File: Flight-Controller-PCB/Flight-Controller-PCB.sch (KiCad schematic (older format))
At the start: 28 parts, among them J1 Power_In, J2 ESC_1, J3 ESC_2, J4 ESC_3, J5 ESC_4, J6 Receiver, J7 Aux, U1 MCP6001U

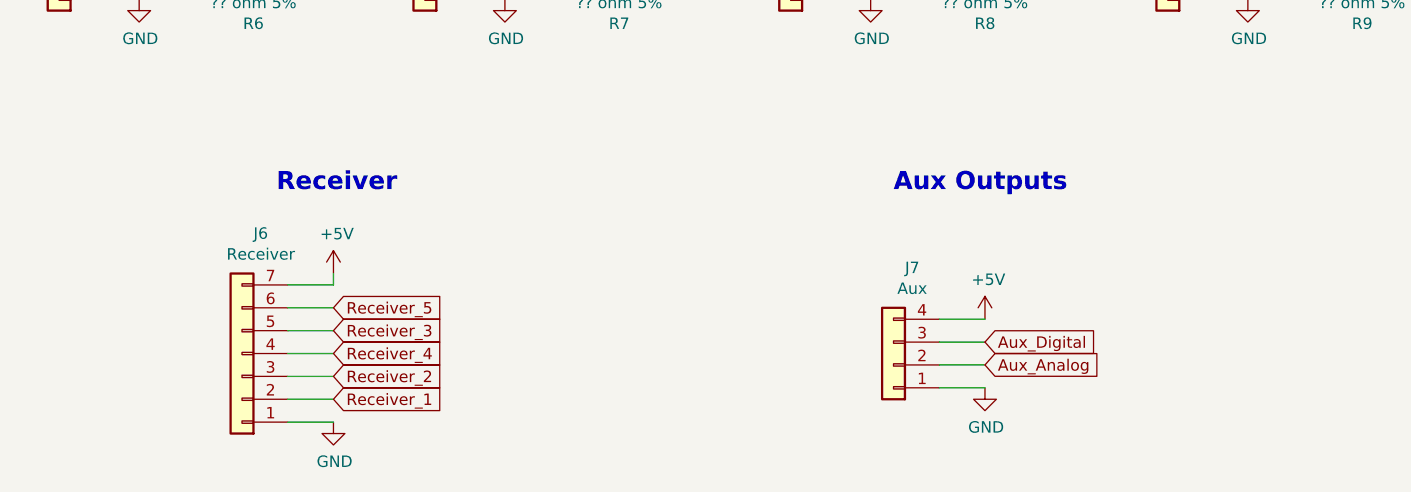
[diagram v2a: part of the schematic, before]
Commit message: Mostly finished off the schematic, need to double check and label
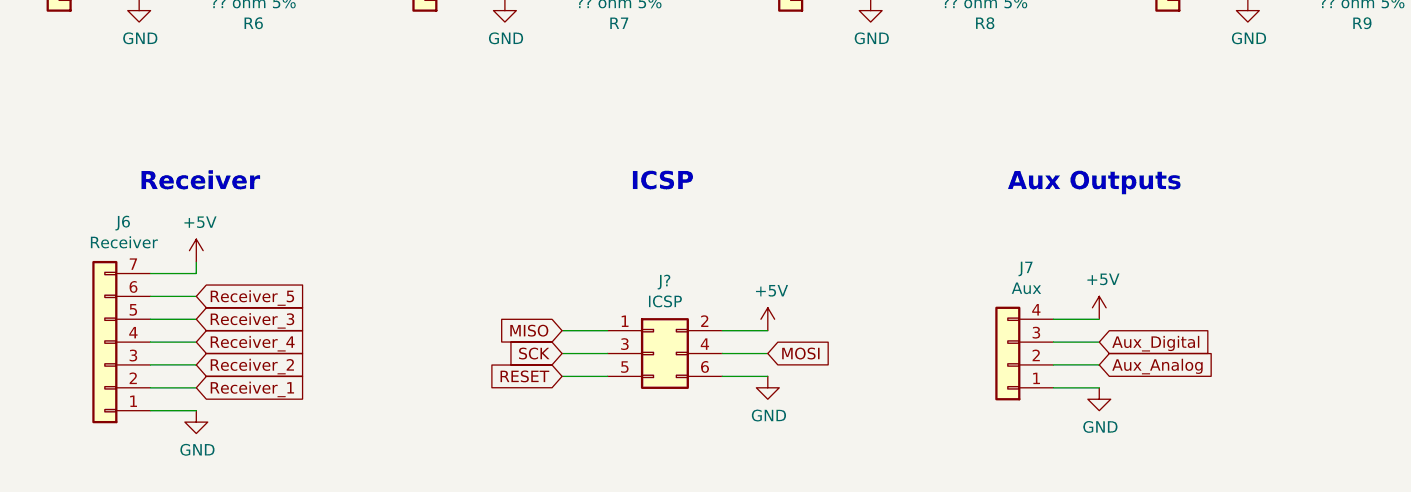
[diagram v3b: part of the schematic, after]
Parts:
- added J?: ICSP, symbol Connector_Generic:Conn_02x03_Odd_Even
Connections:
- net +5V: now also J?.2 (Pin_2)
- net GND: now also J?.6 (Pin_6)
- new net MISO: J?.1 (Pin_1)
- new net MOSI: J?.4 (Pin_4)
- new net RESET: J?.5 (Pin_5)
- new net SCK: J?.3 (Pin_3)
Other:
- note added: "ICSP"
- moved on the sheet: J6, J7
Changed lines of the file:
@@
 EESchema Schematic File Version 4
+LIBS:Flight-Controller-PCB-cache
 EELAYER 30 0
 EELAYER END
@@
 Text Label 1500 4100 0    50   ~ 0
 ESC_4
-Text Notes 1700 6500 0    79   ~ 16
+Text Notes 1100 6500 0    79   ~ 16
 Receiver
-Text GLabel 1950 7400 2    50   Input ~ 0
+Text GLabel 1350 7350 2    50   Input ~ 0
 Receiver_1
-Text GLabel 1950 7300 2    50   Input ~ 0
+Text GLabel 1350 7250 2    50   Input ~ 0
 Receiver_2
-Text GLabel 1950 7100 2    50   Input ~ 0
+Text GLabel 1350 7050 2    50   Input ~ 0
 Receiver_3
-Text GLabel 1950 7200 2    50   Input ~ 0
+Text GLabel 1350 7150 2    50   Input ~ 0
 Receiver_4
 $Comp
 L power:+5V #PWR018
 U 1 1 5FE81BA9
-P 1950 6850
-F 0 "#PWR018" H 1950 6700 50  0001 C CNN
-F 1 "+5V" H 1965 7023 50  0000 C CNN
-F 2 "" H 1950 6850 50  0001 C CNN
-F 3 "" H 1950 6850 50  0001 C CNN
-	1    1950 6850
+P 1350 6800
+F 0 "#PWR018" H 1350 6650 50  0001 C CNN
+F 1 "+5V" H 1365 6973 50  0000 C CNN
+F 2 "" H 1350 6800 50  0001 C CNN
+F 3 "" H 1350 6800 50  0001 C CNN
+	1    1350 6800
 	1    0    0    -1
 $EndComp
@@
 L power:GND #PWR021
 U 1 1 5FE821AC
-P 1950 7500
-F 0 "#PWR021" H 1950 7250 50  0001 C CNN
-F 1 "GND" H 1955 7327 50  0000 C CNN
-F 2 "" H 1950 7500 50  0001 C CNN
-F 3 "" H 1950 7500 50  0001 C CNN
-	1    1950 7500
+P 1350 7450
+F 0 "#PWR021" H 1350 7200 50  0001 C CNN
+F 1 "GND" H 1355 7277 50  0000 C CNN
+F 2 "" H 1350 7450 50  0001 C CNN
+F 3 "" H 1350 7450 50  0001 C CNN
+	1    1350 7450
 	1    0    0    -1
 $EndComp
@@
 Light_4
 Wire Wire Line
-	1750 7500 1950 7500
-Wire Wire Line
-	1750 6900 1950 6900
-Wire Wire Line
-	1950 6900 1950 6850
-Wire Wire Line
-	1750 7400 1950 7400
-Wire Wire Line
-	1750 7300 1950 7300
-Wire Wire Line
-	1950 7100 1750 7100
-Wire Wire Line
-	1750 7200 1950 7200
+	1150 7450 1350 7450
+Wire Wire Line
+	1150 6850 1350 6850
+Wire Wire Line
+	1350 6850 1350 6800
+Wire Wire Line
+	1150 7350 1350 7350
+Wire Wire Line
+	1150 7250 1350 7250
+Wire Wire Line
+	1350 7050 1150 7050
+Wire Wire Line
+	1150 7150 1350 7150
 Wire Wire Line
 	7150 2250 7200 2250
@@
 L Connector_Generic:Conn_01x07 J6
 U 1 1 5FF977CD
-P 1550 7200
-F 0 "J6" H 1468 6675 50  0000 C CNN
-F 1 "Receiver" H 1468 6766 50  0000 C CNN
-F 2 "Connector_JST:JST_GH_BM07B-GHS-TBT_1x07-1MP_P1.25mm_Vertical" H 1550 7200 50  0001 C CNN
-F 3 "~" H 1550 7200 50  0001 C CNN
-F 4 "JST Sales America Inc." H 1550 7200 50  0001 C CNN "Manufacturer"
-F 5 "BM07B-GHS-TBT(LF)(SN)(N)" H 1550 7200 50  0001 C CNN "Manufacturer #"
-F 6 "455-1583-1-ND" H 1550 7200 50  0001 C CNN "Digi-Key #"
-F 7 "https://www.digikey.ca/en/products/detail/jst-sales-america-inc/BM07B-GHS-TBT-LF-SN-N/807805?s=N4IgTCBcDaIEIFkAMB2OBaA4gCQMroBU4CQBdAXyA" H 1550 7200 50  0001 C CNN "Digi-Key LinkDigi LinkDigi-Key Link"
-	1    1550 7200
+P 950 7150
+F 0 "J6" H 868 6625 50  0000 C CNN
+F 1 "Receiver" H 868 6716 50  0000 C CNN
+F 2 "Connector_JST:JST_GH_BM07B-GHS-TBT_1x07-1MP_P1.25mm_Vertical" H 950 7150 50  0001 C CNN
+F 3 "~" H 950 7150 50  0001 C CNN
+F 4 "JST Sales America Inc." H 950 7150 50  0001 C CNN "Manufacturer"
+F 5 "BM07B-GHS-TBT(LF)(SN)(N)" H 950 7150 50  0001 C CNN "Manufacturer #"
+F 6 "455-1583-1-ND" H 950 7150 50  0001 C CNN "Digi-Key #"
+F 7 "https://www.digikey.ca/en/products/detail/jst-sales-america-inc/BM07B-GHS-TBT-LF-SN-N/807805?s=N4IgTCBcDaIEIFkAMB2OBaA4gCQMroBU4CQBdAXyA" H 950 7150 50  0001 C CNN "Digi-Key LinkDigi LinkDigi-Key Link"
+	1    950  7150
 	-1   0    0    1
 $EndComp
-Text Notes 4400 6500 0    79   ~ 16
+Text Notes 4900 6500 0    79   ~ 16
 Aux Outputs
 Text GLabel 3850 4050 0    50   Input ~ 0
@@
 Text Label 4300 4200 0    50   ~ 0
 Aux_Analog
-Text GLabel 4800 7150 2    50   Input ~ 0
+Text GLabel 5300 7150 2    50   Input ~ 0
 Aux_Digital
-Text GLabel 4800 7250 2    50   Input ~ 0
+Text GLabel 5300 7250 2    50   Input ~ 0
 Aux_Analog
 $Comp
 L Connector_Generic:Conn_01x04 J7
 U 1 1 5FFD0529
-P 4400 7250
-F 0 "J7" H 4318 6825 50  0000 C CNN
-F 1 "Aux" H 4318 6916 50  0000 C CNN
-F 2 "Connector_JST:JST_GH_BM04B-GHS-TBT_1x04-1MP_P1.25mm_Vertical" H 4400 7250 50  0001 C CNN
-F 3 "~" H 4400 7250 50  0001 C CNN
-F 4 "JST Sales America Inc." H 4400 7250 50  0001 C CNN "Manufacturer"
-F 5 "BM04B-GHS-TBT(LF)(SN)(N)" H 4400 7250 50  0001 C CNN "Manufacturer #"
-F 6 "455-1580-1-ND" H 4400 7250 50  0001 C CNN "Digi-Key #"
-F 7 "https://www.digikey.ca/en/products/detail/jst-sales-america-inc/BM04B-GHS-TBT-LF-SN-N/807802?s=N4IgTCBcDaIEIFkAMAWOBaA4gCQMroBU4CQBdAXyA" H 4400 7250 50  0001 C CNN "Digi-Key LinkDigi LinkDigi-Key Link"
-	1    4400 7250
+P 4900 7250
+F 0 "J7" H 4818 6825 50  0000 C CNN
+F 1 "Aux" H 4818 6916 50  0000 C CNN
+F 2 "Connector_JST:JST_GH_BM04B-GHS-TBT_1x04-1MP_P1.25mm_Vertical" H 4900 7250 50  0001 C CNN
+F 3 "~" H 4900 7250 50  0001 C CNN
+F 4 "JST Sales America Inc." H 4900 7250 50  0001 C CNN "Manufacturer"
+F 5 "BM04B-GHS-TBT(LF)(SN)(N)" H 4900 7250 50  0001 C CNN "Manufacturer #"
+F 6 "455-1580-1-ND" H 4900 7250 50  0001 C CNN "Digi-Key #"
+F 7 "https://www.digikey.ca/en/products/detail/jst-sales-america-inc/BM04B-GHS-TBT-LF-SN-N/807802?s=N4IgTCBcDaIEIFkAMAWOBaA4gCQMroBU4CQBdAXyA" H 4900 7250 50  0001 C CNN "Digi-Key LinkDigi LinkDigi-Key Link"
+	1    4900 7250
 	-1   0    0    1
 $EndComp
@@
 L power:GND #PWR020
 U 1 1 5FFD3AC4
-P 4800 7350
-F 0 "#PWR020" H 4800 7100 50  0001 C CNN
-F 1 "GND" H 4805 7177 50  0000 C CNN
-F 2 "" H 4800 7350 50  0001 C CNN
-F 3 "" H 4800 7350 50  0001 C CNN
-	1    4800 7350
+P 5300 7350
+F 0 "#PWR020" H 5300 7100 50  0001 C CNN
+F 1 "GND" H 5305 7177 50  0000 C CNN
+F 2 "" H 5300 7350 50  0001 C CNN
+F 3 "" H 5300 7350 50  0001 C CNN
+	1    5300 7350
 	1    0    0    -1
 $EndComp
@@
 L power:+5V #PWR019
 U 1 1 5FFD70B9
-P 4800 7050
-F 0 "#PWR019" H 4800 6900 50  0001 C CNN
-F 1 "+5V" H 4815 7223 50  0000 C CNN
-F 2 "" H 4800 7050 50  0001 C CNN
-F 3 "" H 4800 7050 50  0001 C CNN
-	1    4800 7050
-	1    0    0    -1
-$EndComp
-Wire Wire Line
-	4600 7050 4800 7050
-Wire Wire Line
-	4600 7350 4800 7350
-Wire Wire Line
-	4600 7250 4800 7250
-Wire Wire Line
-	4600 7150 4800 7150
+P 5300 7050
+F 0 "#PWR019" H 5300 6900 50  0001 C CNN
+F 1 "+5V" H 5315 7223 50  0000 C CNN
+F 2 "" H 5300 7050 50  0001 C CNN
+F 3 "" H 5300 7050 50  0001 C CNN
+	1    5300 7050
+	1    0    0    -1
+$EndComp
+Wire Wire Line
+	5100 7050 5300 7050
+Wire Wire Line
+	5100 7350 5300 7350
+Wire Wire Line
+	5100 7250 5300 7250
+Wire Wire Line
+	5100 7150 5300 7150
 $Comp
 L Connector_Generic:Conn_01x06 J1
@@
 Text Label 4350 3050 0    50   ~ 0
 Receiver_4
-Text GLabel 1950 7000 2    50   Input ~ 0
+Text GLabel 1350 6950 2    50   Input ~ 0
 Receiver_5
 Wire Wire Line
-	1750 7000 1950 7000
+	1150 6950 1350 6950
 Text Notes 7900 3450 0    79   ~ 16
 Master Indicator LEDs
@@
 Wire Wire Line
 	7750 5150 8450 5150
+$Comp
+L Connector_Generic:Conn_02x03_Odd_Even J?
+U 1 1 6036A900
+P 3350 7200
+AR Path="/5FDD4B9C/6036A900" Ref="J?"  Part="1"
+AR Path="/6036A900" Ref="J?"  Part="1"
+F 0 "J?" H 3400 7517 50  0000 C CNN
+F 1 "ICSP" H 3400 7426 50  0000 C CNN
+F 2 "" H 3350 7200 50  0001 C CNN
+F 3 "~" H 3350 7200 50  0001 C CNN
+	1    3350 7200
+	1    0    0    -1
+$EndComp
+Text GLabel 2950 7100 0    50   Input ~ 0
+MISO
+Text GLabel 3850 7200 2    50   Input ~ 0
+MOSI
+Text GLabel 2950 7200 0    50   Input ~ 0
+SCK
+$Comp
+L power:+5V #PWR?
+U 1 1 6036A909
+P 3850 7100
+AR Path="/5FDD4B9C/6036A909" Ref="#PWR?"  Part="1"
+AR Path="/6036A909" Ref="#PWR?"  Part="1"
+F 0 "#PWR?" H 3850 6950 50  0001 C CNN
+F 1 "+5V" H 3865 7273 50  0000 C CNN
+F 2 "" H 3850 7100 50  0001 C CNN
+F 3 "" H 3850 7100 50  0001 C CNN
+	1    3850 7100
+	1    0    0    -1
+$EndComp
+$Comp
+L power:GND #PWR?
+U 1 1 6036A90F
+P 3850 7300
+AR Path="/5FDD4B9C/6036A90F" Ref="#PWR?"  Part="1"
+AR Path="/6036A90F" Ref="#PWR?"  Part="1"
+F 0 "#PWR?" H 3850 7050 50  0001 C CNN
+F 1 "GND" H 3855 7127 50  0000 C CNN
+F 2 "" H 3850 7300 50  0001 C CNN
+F 3 "" H 3850 7300 50  0001 C CNN
+	1    3850 7300
+	1    0    0    -1
+$EndComp
+Wire Wire Line
+	3650 7100 3850 7100
+Wire Wire Line
+	3850 7200 3650 7200
+Wire Wire Line
+	3650 7300 3850 7300
+Wire Wire Line
+	2950 7100 3150 7100
+Text GLabel 2950 7300 0    50   Input ~ 0
+RESET
+Wire Wire Line
+	2950 7300 3150 7300
+Wire Wire Line
+	3150 7200 2950 7200
+Text Notes 3250 6500 0    79   ~ 16
+ICSP
 $EndSCHEMATC

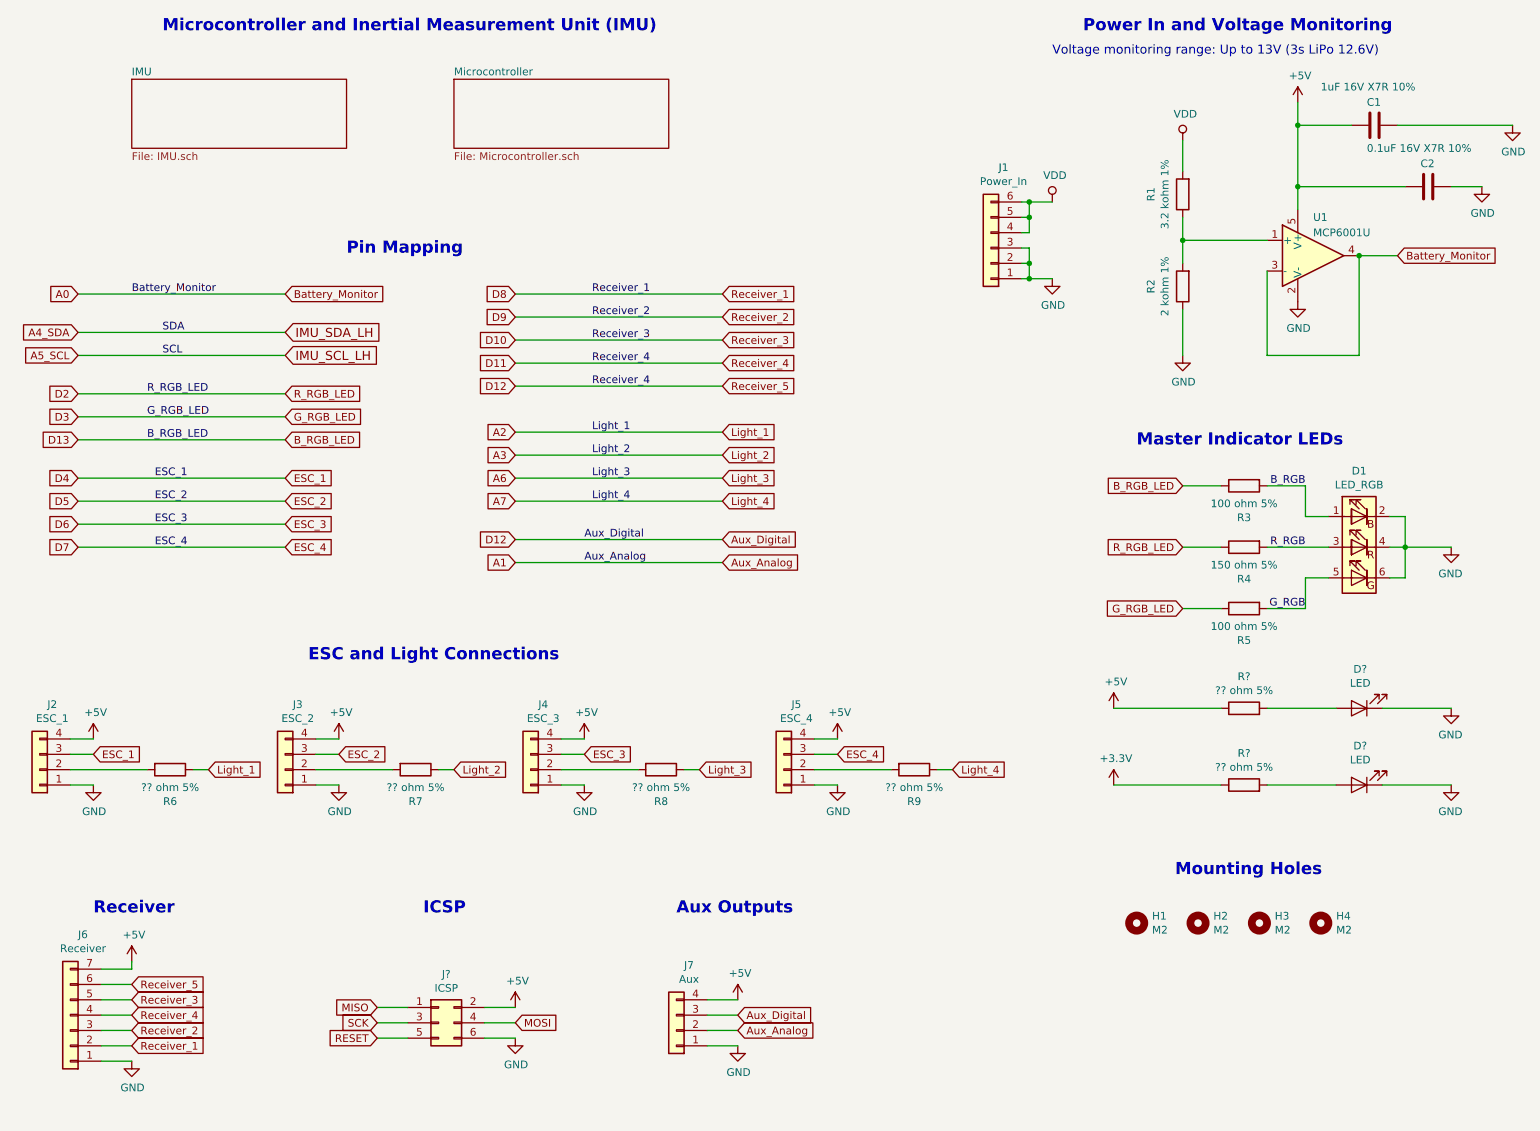
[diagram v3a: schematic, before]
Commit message: Updated pin mappings
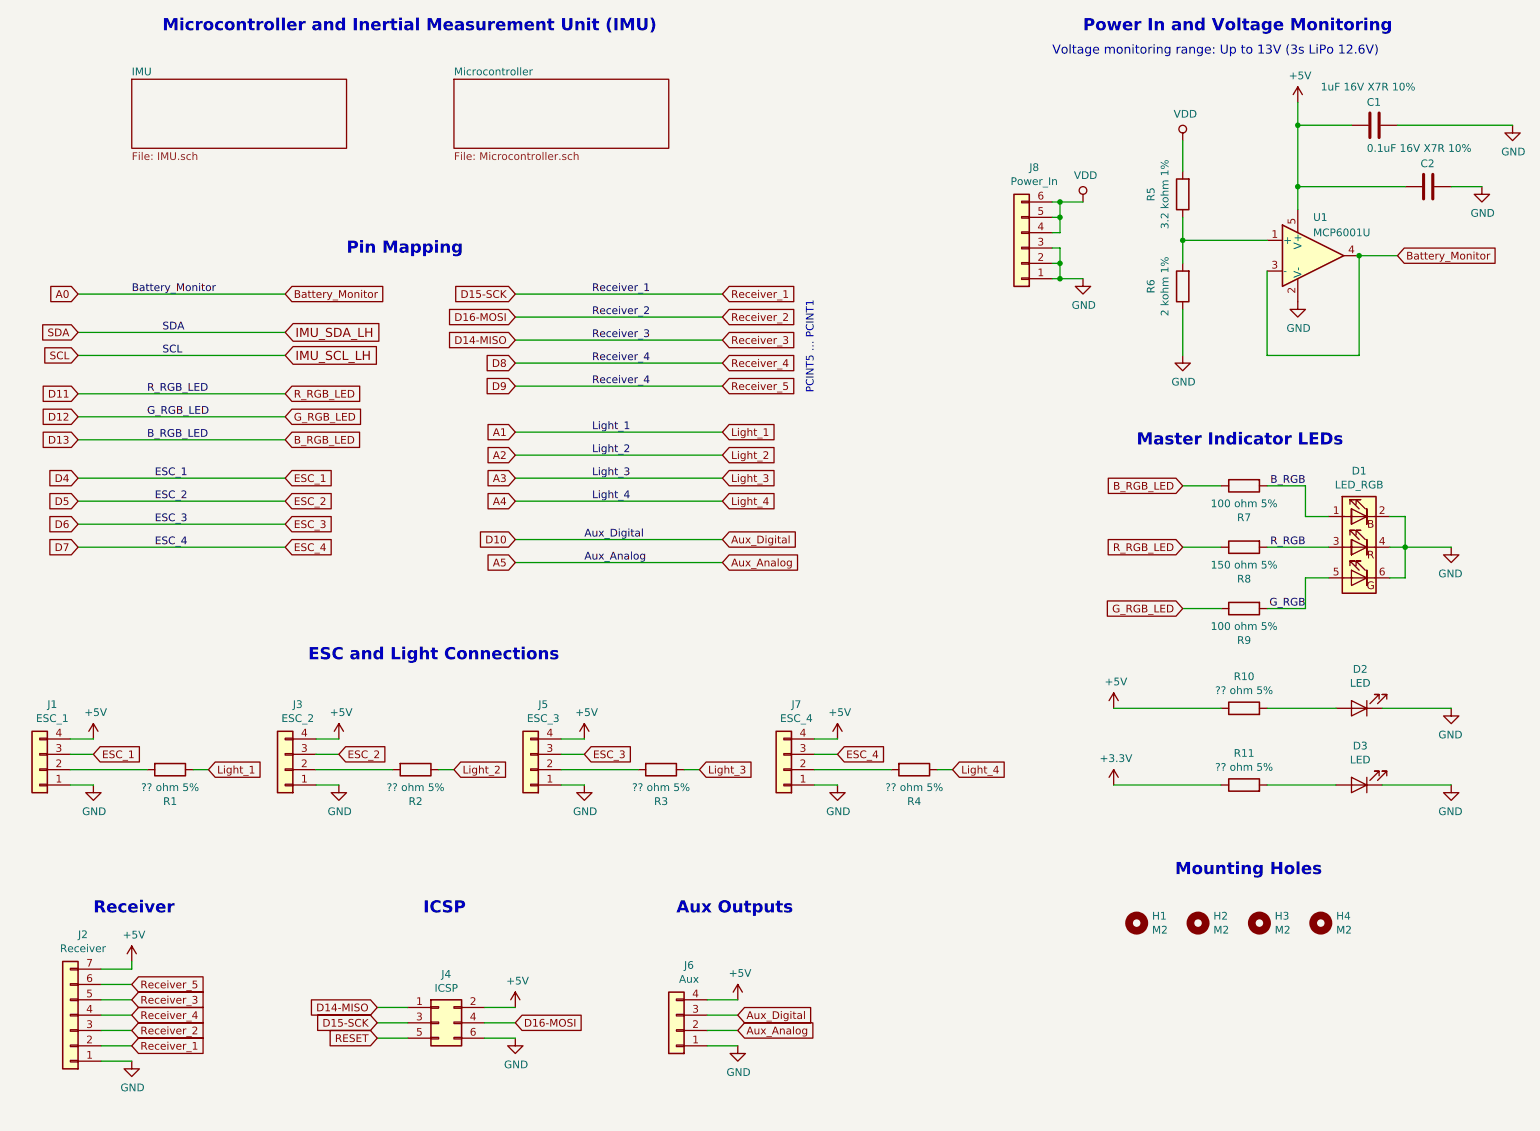
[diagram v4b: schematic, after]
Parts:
- gave numbers to parts that had none: 5
- renumbered J2 to J1, J6 to J2, J4 to J5, J7 to J6, J5 to J7, J1 to J8, R6 to R1, R7 to R2, R8 to R3, R9 to R4, R1 to R5, R2 to R6, R3 to R7, R4 to R8, R5 to R9
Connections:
- net A6 is gone; now on net A3: R3.1
- net MISO is gone; now on net D14-MISO: J4.1 (Pin_1)
- net MOSI is gone; now on net D16-MOSI: J4.4 (Pin_4)
- net A1: now also R1.1; no longer J6.2 (Pin_2)
- net A2: now also R2.1; no longer R1.1
- net A3: no longer R2.1
- net Aux_Digital: no longer J2.4 (Pin_4), J2.6 (Pin_6)
- net D8: now also J2.4 (Pin_4), J2.6 (Pin_6); no longer J2.2 (Pin_2)
- net A7 renamed A4
- net D10 renamed D14-MISO
- net D2 renamed D11
- net D3 renamed D12
- net D9 renamed D16-MOSI
- net SCK renamed D15-SCK
- net D15-SCK: now also J2.2 (Pin_2)
- new net A5: J6.2 (Pin_2)
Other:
- note added: "PCINT5 … PCINT1"
- moved on the sheet: J8
